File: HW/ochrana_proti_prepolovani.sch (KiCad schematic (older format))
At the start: 2 parts

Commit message: add some codes for JLCPCB, change package and schematic of CP2102
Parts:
- R?: LCSC (none) -> C25744
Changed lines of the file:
@@
 F 2 "Resistor_SMD:R_0402_1005Metric" V 5380 3050 50  0001 C CNN
 F 3 "~" H 5450 3050 50  0001 C CNN
+F 4 "C25744" H 5450 3050 50  0001 C CNN "LCSC"
 	1    5450 3050
 	1    0    0    -1

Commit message: add some codes for JLCPCB
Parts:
- Q?: LCSC (none) -> C15127
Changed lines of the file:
@@
 F 2 "Package_TO_SOT_SMD:SOT-23" H 5650 2650 50  0001 C CNN
 F 3 "~" H 5450 2550 50  0001 C CNN
+F 4 "C15127" H 5450 2550 50  0001 C CNN "LCSC"
 	1    5450 2550
 	0    -1   -1   0

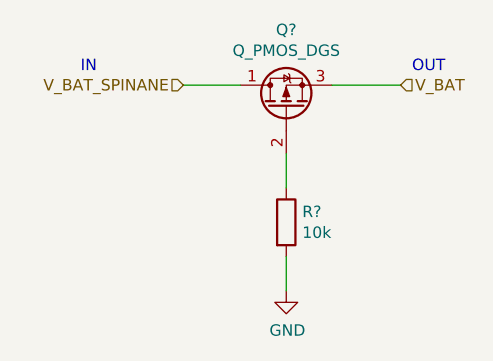
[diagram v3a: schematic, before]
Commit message: numbering components, place components on board
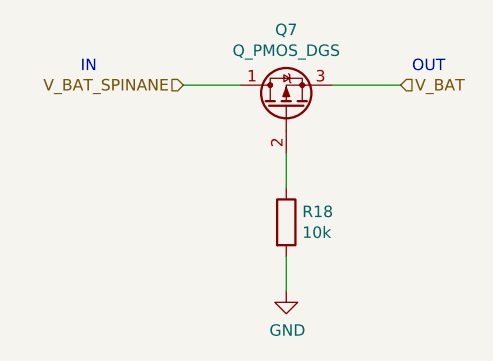
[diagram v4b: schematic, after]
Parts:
- gave numbers to parts that had none: 2
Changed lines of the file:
@@
 AR Path="/5F7BA54B/5F7BCC0A/5F76D204" Ref="Q?"  Part="1"
 AR Path="/5F7BA54B/5F7BCC69/5F76D204" Ref="Q?"  Part="1"
-AR Path="/5F76D05B/5F76D204" Ref="Q?"  Part="1"
-F 0 "Q?" V 5792 2550 50  0000 C CNN
+AR Path="/5F76D05B/5F76D204" Ref="Q7"  Part="1"
+F 0 "Q7" V 5792 2550 50  0000 C CNN
 F 1 "Q_PMOS_DGS" V 5701 2550 50  0000 C CNN
 F 2 "Package_TO_SOT_SMD:SOT-23" H 5650 2650 50  0001 C CNN
@@
 AR Path="/5F7BA54B/5F7BCC0A/5F76D20A" Ref="R?"  Part="1"
 AR Path="/5F7BA54B/5F7BCC69/5F76D20A" Ref="R?"  Part="1"
-AR Path="/5F76D05B/5F76D20A" Ref="R?"  Part="1"
-F 0 "R?" H 5520 3096 50  0000 L CNN
+AR Path="/5F76D05B/5F76D20A" Ref="R18"  Part="1"
+F 0 "R18" H 5520 3096 50  0000 L CNN
 F 1 "10k" H 5520 3005 50  0000 L CNN
 F 2 "Resistor_SMD:R_0402_1005Metric" V 5380 3050 50  0001 C CNN
@@
 V_BAT
 $Comp
-L power:GND #PWR?
+L power:GND #PWR0314
 U 1 1 5F76D2C3
 P 5450 3350
-F 0 "#PWR?" H 5450 3100 50  0001 C CNN
+F 0 "#PWR0314" H 5450 3100 50  0001 C CNN
 F 1 "GND" H 5455 3177 50  0000 C CNN
 F 2 "" H 5450 3350 50  0001 C CNN

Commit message: ready for first prototype
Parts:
- Q7: JLCPCB_CORRECTION (none) -> 0;0;180
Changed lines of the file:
@@
 F 3 "~" H 5450 2550 50  0001 C CNN
 F 4 "C15127" H 5450 2550 50  0001 C CNN "LCSC"
+F 5 "0;0;180" H 5450 2550 50  0001 C CNN "JLCPCB_CORRECTION"
 	1    5450 2550
 	0    -1   -1   0
